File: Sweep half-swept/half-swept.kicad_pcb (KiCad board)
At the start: 2 copper layers, 109 x 86.6 mm, 25 parts, among them J2 AudioJack4dpb, SW1 SW_Push, SW10 SW_Push, SW11 SW_Push, SW12 SW_Push, SW13 SW_Push, SW14 SW_Push, SW15 SW_Push, SW16 SW_Push, SW17 SW_Push, SW2 SW_Push, SW3 SW_Push, SW4 SW_Push, SW5 SW_Push, SW6 SW_Push, SW7 SW_Push, SW8 SW_Push, SW9 SW_Push, U1 ProMicro-kbd

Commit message: Add RTIC logo
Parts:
- added G***: LOGO, Sweep half-swept:rtic, F.Cu at (63.2, 78.5)

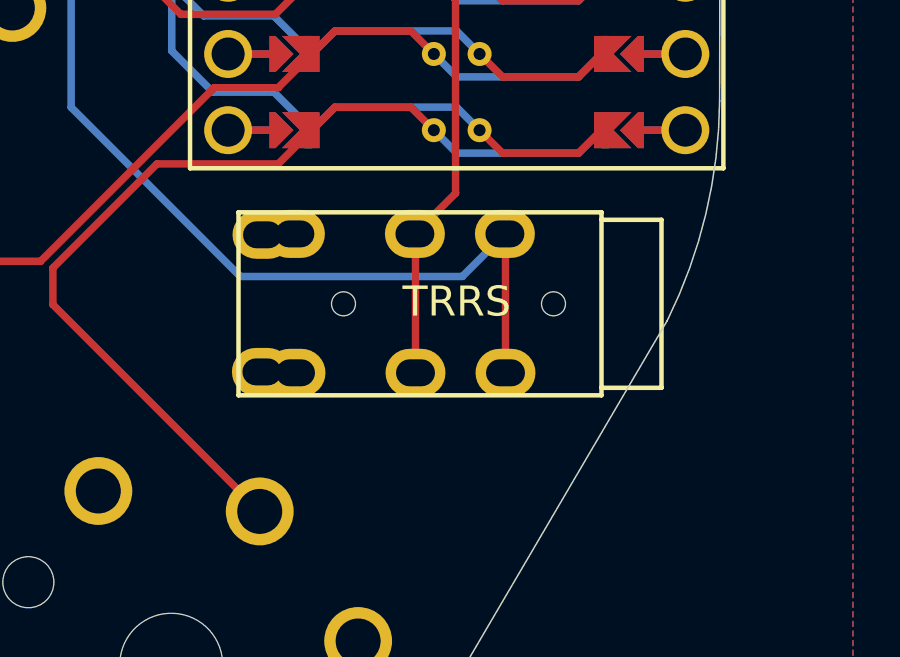
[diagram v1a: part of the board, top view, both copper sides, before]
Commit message: Cleanup TRRS and add Rust logo
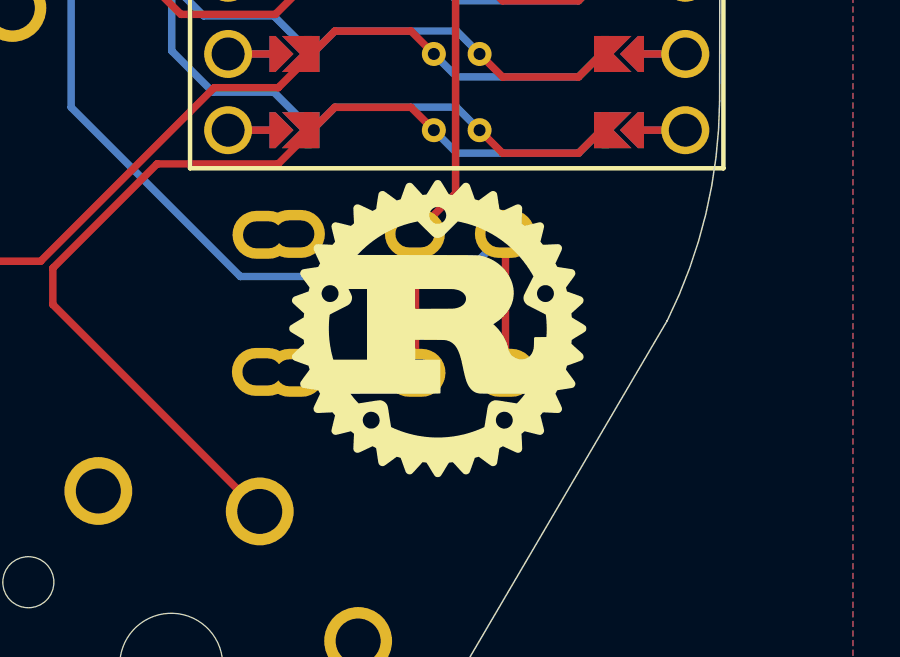
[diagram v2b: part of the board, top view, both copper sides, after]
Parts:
- added G***: LOGO, Sweep half-swept:rust, F.Cu at (118.2, 83.6)
- added G***: LOGO, Sweep half-swept:rust, B.Cu at (118.2, 83.6)
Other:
- board text removed: "TRRS"

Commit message: Round tracks plugin
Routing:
- net Switch6: track 126.9 -> 123.7 mm
- net Switch2: track 94.9 -> 92.0 mm
- net Switch1: track 102.8 -> 100.2 mm
- net Switch3: track 73.0 -> 70.7 mm
- net Switch11: track 107.5 -> 105.3 mm
- net Switch7: track 84.4 -> 82.2 mm
- net Switch8: track 61.8 -> 60.0 mm
- net reset: track 49.7 -> 48.1 mm
- net BT+_r: track 50.6 -> 49.1 mm
- net Switch12: track 82.6 -> 81.2 mm
- net Switch4: track 49.1 -> 47.7 mm
- net Switch13: track 58.5 -> 57.2 mm
- net Switch9: track 43.6 -> 42.4 mm
- net Switch14: track 43.3 -> 42.2 mm
- net raw: track 42.9 -> 42.0 mm
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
